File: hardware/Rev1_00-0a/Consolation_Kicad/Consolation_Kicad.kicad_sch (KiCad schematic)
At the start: 0 parts

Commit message: Update block diagram for battery charger + power delivery solution based on BQ25640 Start Pinout documentation for RP2350-based joystick controller Create new schematic pages
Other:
- added sheet CM5_CONN_A (RPI_CM5_A.kicad_sch)
- added sheet CM5_CONN_B (RPI_CM5_B.kicad_sch)
- added sheet DSI TO LVDS (DSI TO LVDS.kicad_sch)
- added sheet TFT CONN (TFT CONN.kicad_sch)
- added sheet TYPE C CHARGER (TYPE C CHARGER.kicad_sch)
- added sheet USB2 MUX (USB2 MUX.kicad_sch)
- added sheet USB3 (USB3.kicad_sch)
- note added: "Resistors are 1% 1/16W 0402 unless otherwise noted Capacitors are 10% 50V X7R 0402 unless otherwise noted"

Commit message: Work on block diagram
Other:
- removed sheet USB2 MUX
- added sheet CONTROLLER (CONTROLLER.kicad_sch)
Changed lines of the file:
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@@
+	)
+	(sheet
+		(at 137.795 38.1)
+		(size 12.7 3.81)
+		(exclude_from_sim no)
+		(in_bom yes)
+		(on_board yes)
+		(dnp no)
+		(fields_autoplaced yes)
+		(stroke
+			(width 0.1524)
+			(type solid)
+		)
+		(fill
+			(color 0 0 0 0)
+		)
+		(property "Sheetname" "CONTROLLER"
+			(at 137.795 37.3884 0)
+			(show_name no)
+			(do_not_autoplace no)
+			(effects
+				(font
+					(size 1.27 1.27)
+				)
+				(justify left bottom)
+			)
+		)
+		(property "Sheetfile" "CONTROLLER.kicad_sch"
+			(at 137.795 42.4946 0)
+			(show_name no)
+			(do_not_autoplace no)
+			(effects
+				(font
+					(size 1.27 1.27)
+				)
+				(justify left top)
+			)
+		)
+		(instances
+			(project "Consolation_Kicad"
+				(path "/b18b5a64-cfe0-4447-acaf-556f3c6e6513"
+					(page "9")
+				)
+			)
+		)
 	)
 	(sheet
@@
 				)
 			)
-		)
-	)
-	(sheet
-		(at 126.365 62.865)
-		(size 13.335 4.445)
-		(exclude_from_sim no)
-		(in_bom yes)
-		(on_board yes)
-		(dnp no)
-		(fields_autoplaced yes)
-		(stroke
-			(width 0.1524)
-			(type solid)
-		)
-		(fill
-			(color 0 0 0 0)
-		)
-		(property "Sheetname" "USB2 MUX"
-			(at 126.365 62.1534 0)
-			(show_name no)
-			(do_not_autoplace no)
-			(effects
-				(font
-					(size 1.27 1.27)
-				)
-				(justify left bottom)
-			)
-		)
-		(property "Sheetfile" "USB2 MUX.kicad_sch"
-			(at 126.365 67.8946 0)
-			(show_name no)
-			(do_not_autoplace no)
-			(effects
-				(font
-					(size 1.27 1.27)
-				)
-				(justify left top)
-			)
-		)
-		(instances
-			(project "Consolation_Kicad"
-				(path "/b18b5a64-cfe0-4447-acaf-556f3c6e6513"
-					(page "4")
-				)
-			)

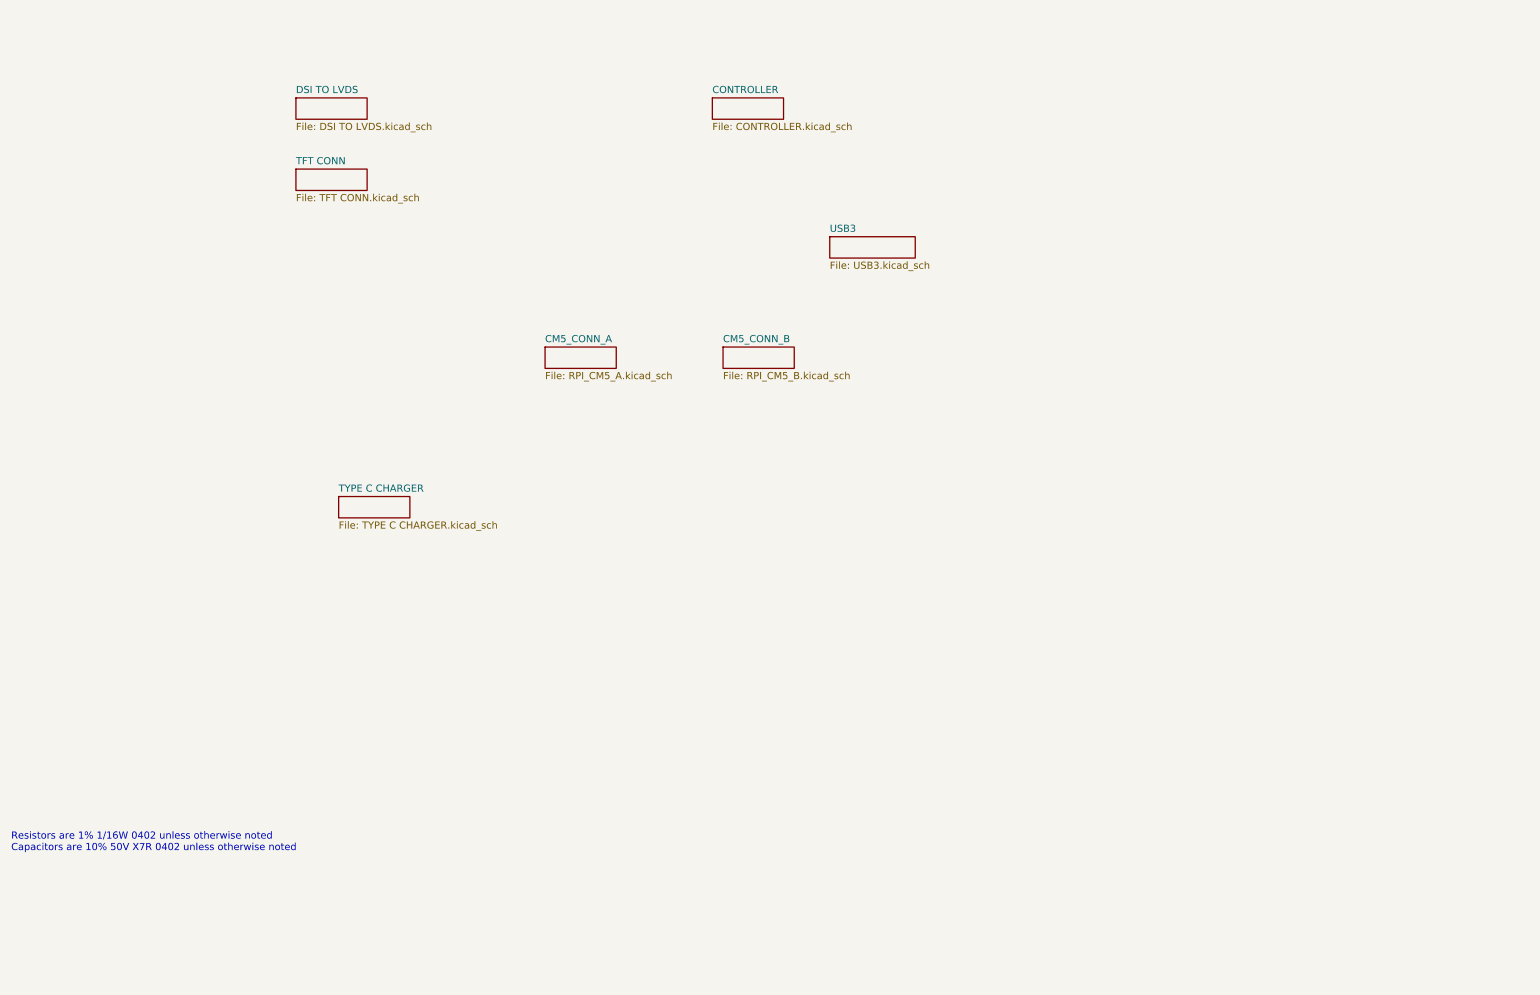
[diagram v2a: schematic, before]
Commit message: Add part number of codec to block diagram Add codec and hdmi schematic sheets
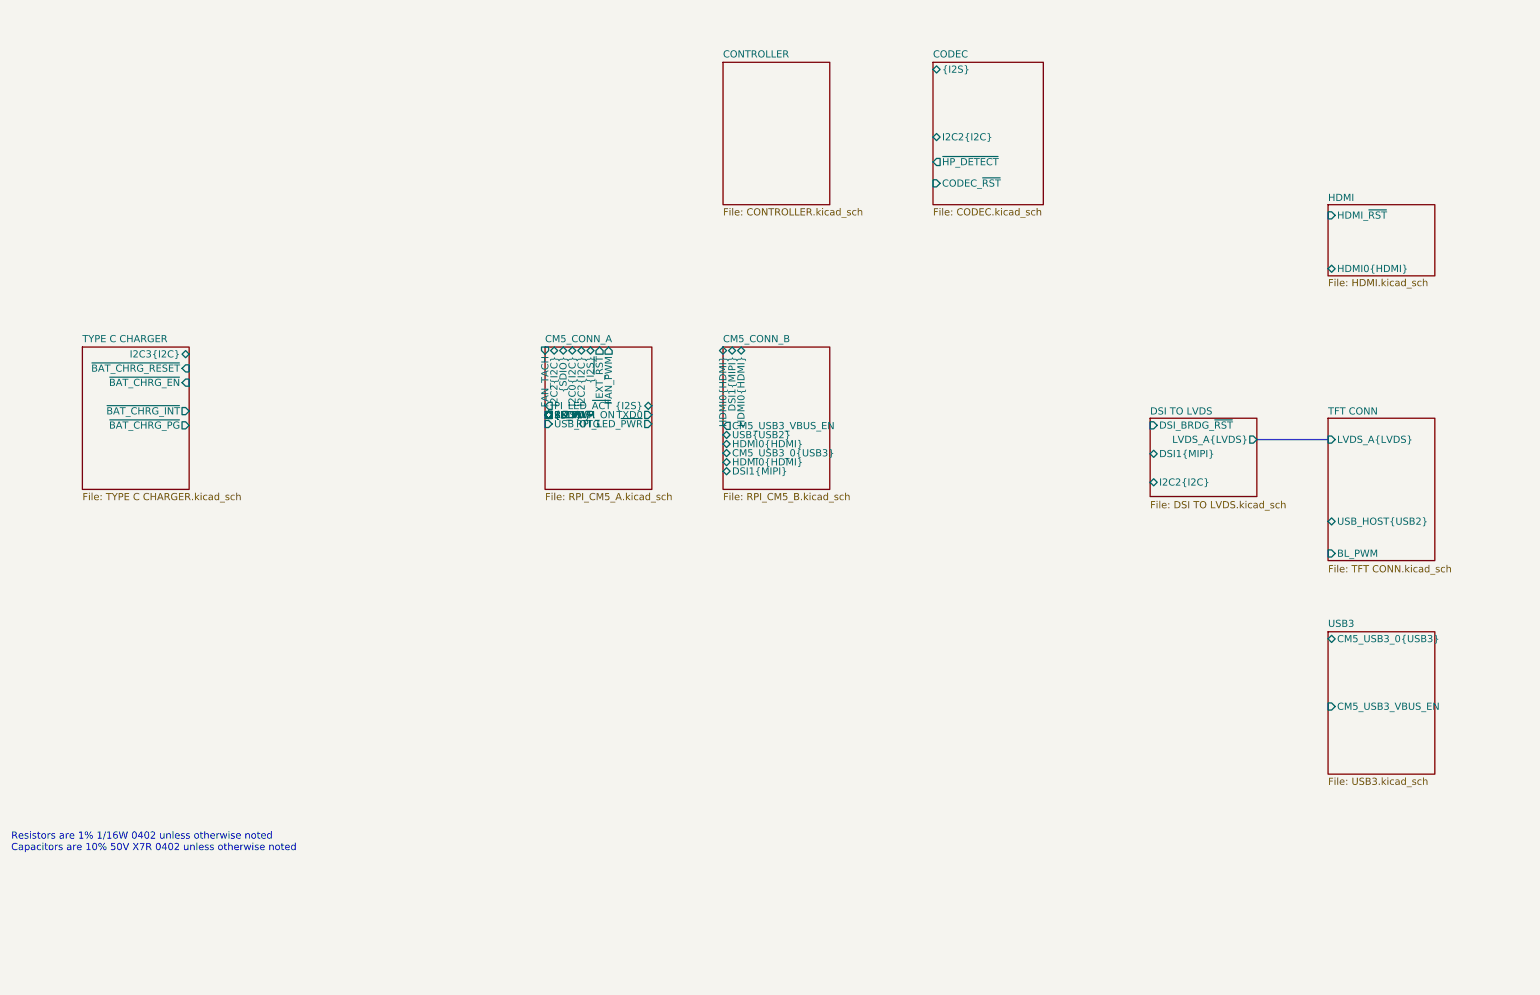
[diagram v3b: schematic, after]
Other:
- added sheet CODEC (CODEC.kicad_sch)
- added sheet HDMI (HDMI.kicad_sch)
- sheet CM5_CONN_A ports: added BL_PWM, EXT_~{RST}, FAN_PWM, FAN_TACH, I2C0{I2C}, I2C2{I2C}, PI_LED_~{ACT}, RPI_LED_~{PWR}, RXD0, SD_PWR_ON, TXD0, USB_OTG, {I2S}, {SDIO}; removed none
- sheet CM5_CONN_B ports: added CM5_USB3_0{USB3}, CM5_USB3_VBUS_EN, DSI1{MIPI}, HDMI0{HDMI}, USB{USB2}; removed none
- sheet DSI TO LVDS ports: added DSI1{MIPI}, DSI_BRDG_~{RST}, I2C2{I2C}, LVDS_A{LVDS}; removed none
- sheet TFT CONN ports: added BL_PWM, LVDS_A{LVDS}, USB_HOST{USB2}; removed none
- sheet TYPE C CHARGER ports: added I2C3{I2C}, ~{BAT_CHRG_EN}, ~{BAT_CHRG_INT}, ~{BAT_CHRG_PG}, ~{BAT_CHRG_RESET}; removed none
- sheet USB3 ports: added CM5_USB3_0{USB3}, CM5_USB3_VBUS_EN; removed none

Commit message: Update schematics, block diagram and pin mux (good progress G)
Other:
- added sheet USB2 MUX (USB2 MUX.kicad_sch)
- sheet CM5_CONN_A ports: added ~{BAT_CHRG_INT}; removed none
- sheet CM5_CONN_B ports: added USB2_NATIVE{USB2}, USB2_RP2350{USB2}; removed USB{USB2}
- sheet TFT CONN ports: added USB2_CTP{USB2}; removed USB_HOST{USB2}
- sheet USB3 ports: added RP2350_USB_VBUS; removed none

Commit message: Update PinMux & Schematics
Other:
- sheet CM5_CONN_A ports: added ~{HP_DETECT}, ~{VOL_DOWN}, ~{VOL_UP}; removed I2C0{I2C}
- sheet CODEC ports: added none; removed ~{HP_DETECT}
- sheet CONTROLLER ports: added I2C2{I2C}, RP2350_RXD0, RP2350_TXD0, RP2350_USB_VBUS, USB_RP2350{USB2}, ~{RP2350_RESET}, ~{RP2350_USB_BOOT}; removed none
- sheet TYPE C CHARGER ports: added I2C2{I2C}; removed I2C3{I2C}

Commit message: ConJoy mostly ready for alpha prototype. Confirm few other potential tweaks at 3d printing
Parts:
- added FID1, FID2, FID3, FID4, FID5, FID6: (no value), footprint:FIDUCIAL, symbol KiCad_Lib_Symbols:FIDUCIAL
- added HOLE5, HOLE6, HOLE7: (no value), footprint:NPTH_M2, symbol KiCad_Lib_Symbols:NPTH_M2
- added TP10, TP11, TP4, TP5, TP6, TP7, TP8, TP9: (no value), symbol KiCad_Lib_Symbols:SMT_TP_100_MILS
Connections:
- new net GND: TP10.1, TP11.1, TP4.1, TP5.1, TP6.1, TP7.1, TP8.1, TP9.1
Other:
- added sheet SD_CARD (SD_CARD.kicad_sch)
- added sheet USB2_PROG (USB2_PROG.kicad_sch)

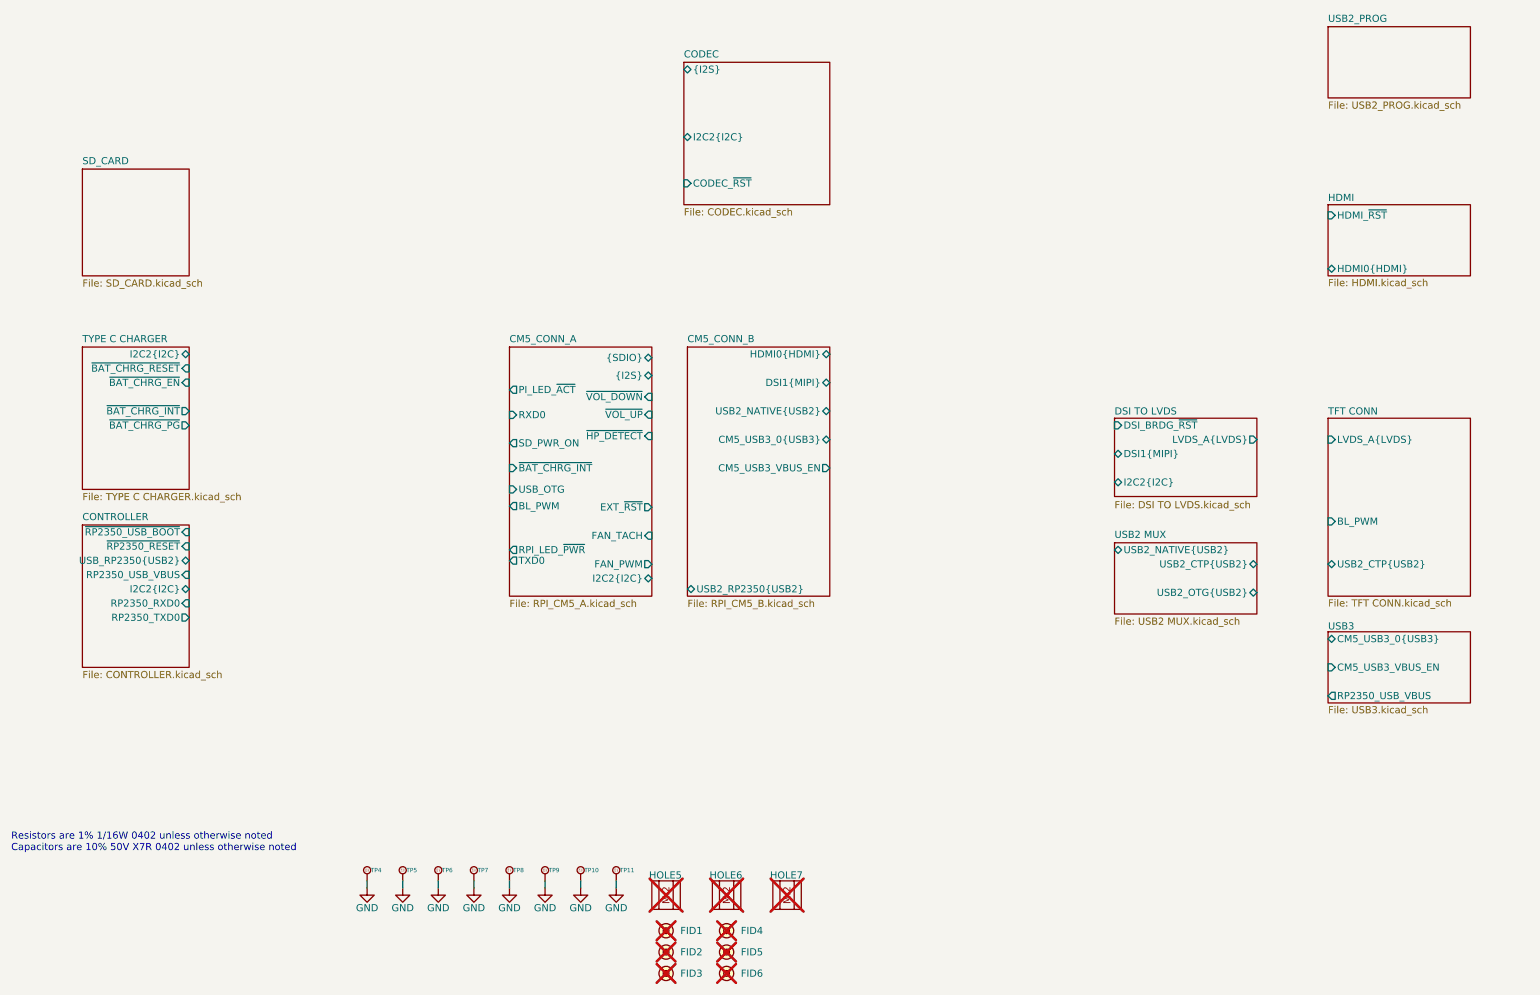
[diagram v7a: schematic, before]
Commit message: Work on block diagram and top-level schematic sheet Work on PinMux
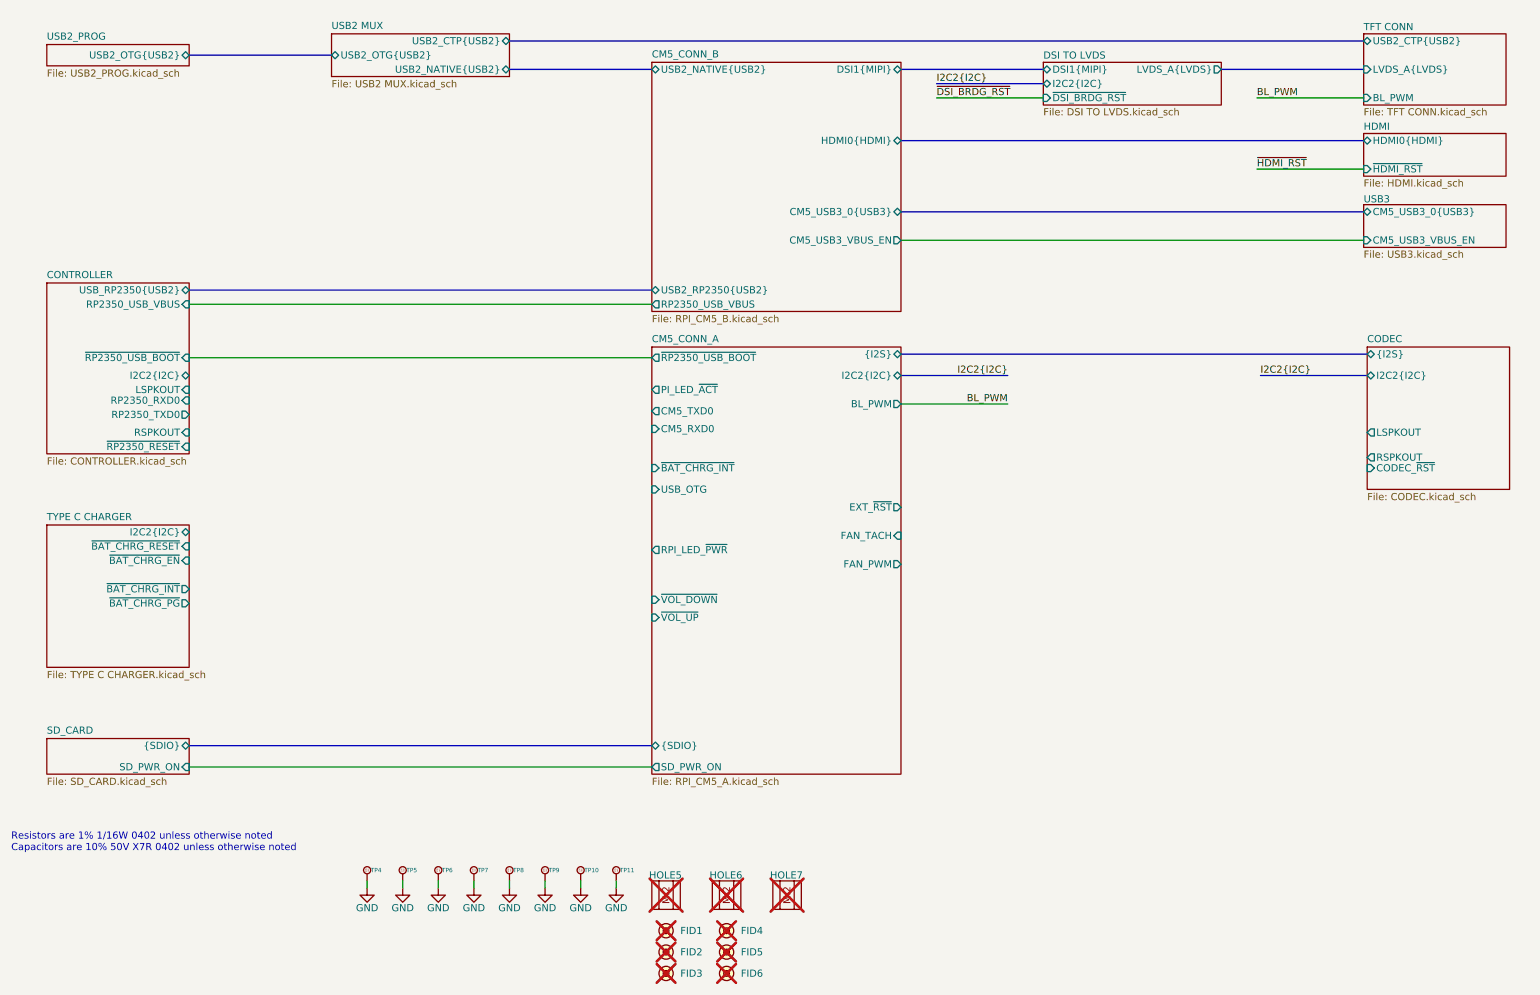
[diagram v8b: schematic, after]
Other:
- sheet CM5_CONN_A ports: added CM5_RXD0, CM5_TXD0, ~{RP2350_USB_BOOT}; removed RXD0, TXD0, ~{HP_DETECT}
- sheet CM5_CONN_B ports: added RP2350_USB_VBUS; removed none
- sheet CODEC ports: added LSPKOUT, RSPKOUT; removed none
- sheet CONTROLLER ports: added LSPKOUT, RSPKOUT; removed none
- sheet DSI TO LVDS ports: added ~{DSI_BRDG_RST}; removed DSI_BRDG_~{RST}
- sheet HDMI ports: added ~{HDMI_RST}; removed HDMI_~{RST}
- sheet SD_CARD ports: added SD_PWR_ON, {SDIO}; removed none
- sheet USB2_PROG ports: added USB2_OTG{USB2}; removed none
- sheet USB3 ports: added none; removed RP2350_USB_VBUS
